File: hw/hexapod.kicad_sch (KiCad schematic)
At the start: 76 parts, among them J1 Supply Motor, J10 Conn_01x03_Pin, J11 Conn_01x03_Pin, J12 Conn_01x03_Pin, J13 Conn_01x03_Pin, J14 Conn_01x03_Pin, J15 Conn_01x03_Pin, J16 Conn_01x03_Pin, J17 Conn_01x03_Pin, J18 Conn_01x03_Pin, J19 Conn_01x03_Pin, J20 Conn_01x03_Pin, J21 Conn_01x03_Pin, J22 Conn_01x03_Pin, J23 Conn_01x03_Pin, J24 Conn_01x03_Pin, J25 Conn_01x03_Pin, J26 Conn_01x03_Pin, J27 Conn_01x03_Pin, J28 Conn_01x03_Pin, J29 Conn_01x03_Pin, J3 Conn_01x03_Pin, J30 Conn_01x03_Pin, J31 Conn_01x03_Pin, J32 Conn_01x03_Pin, J33 Conn_01x03_Pin, J34 Conn_01x03_Pin, J35 Conn_01x06_Pin, J4 Conn_01x03_Pin, J5 Conn_01x03_Pin, J6 Conn_01x03_Pin, J7 Conn_01x03_Pin, J8 Conn_01x03_Pin, J9 Conn_01x03_Pin, Q2 AOD417, U2 PCA9685PW, U3 PCA9685PW

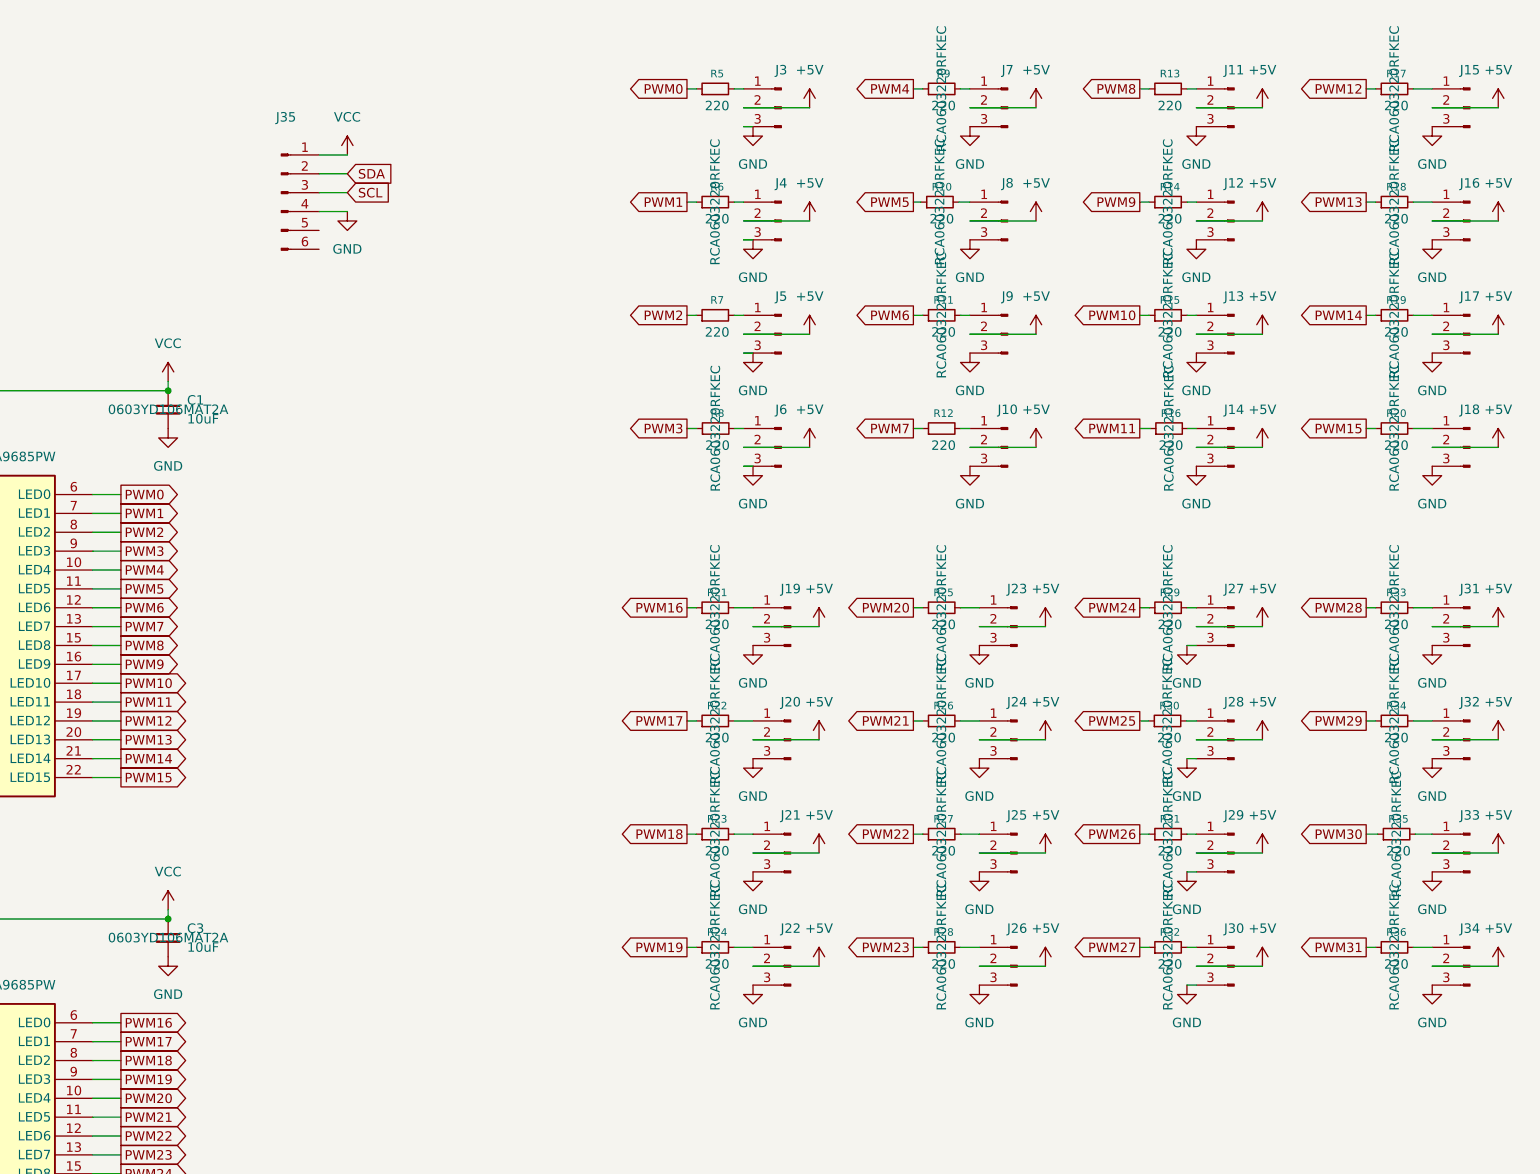
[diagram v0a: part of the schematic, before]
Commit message: hw: Keep only needed pwm
Signed-off-by: Florian Depraz <florian.depraz@outlook.com>
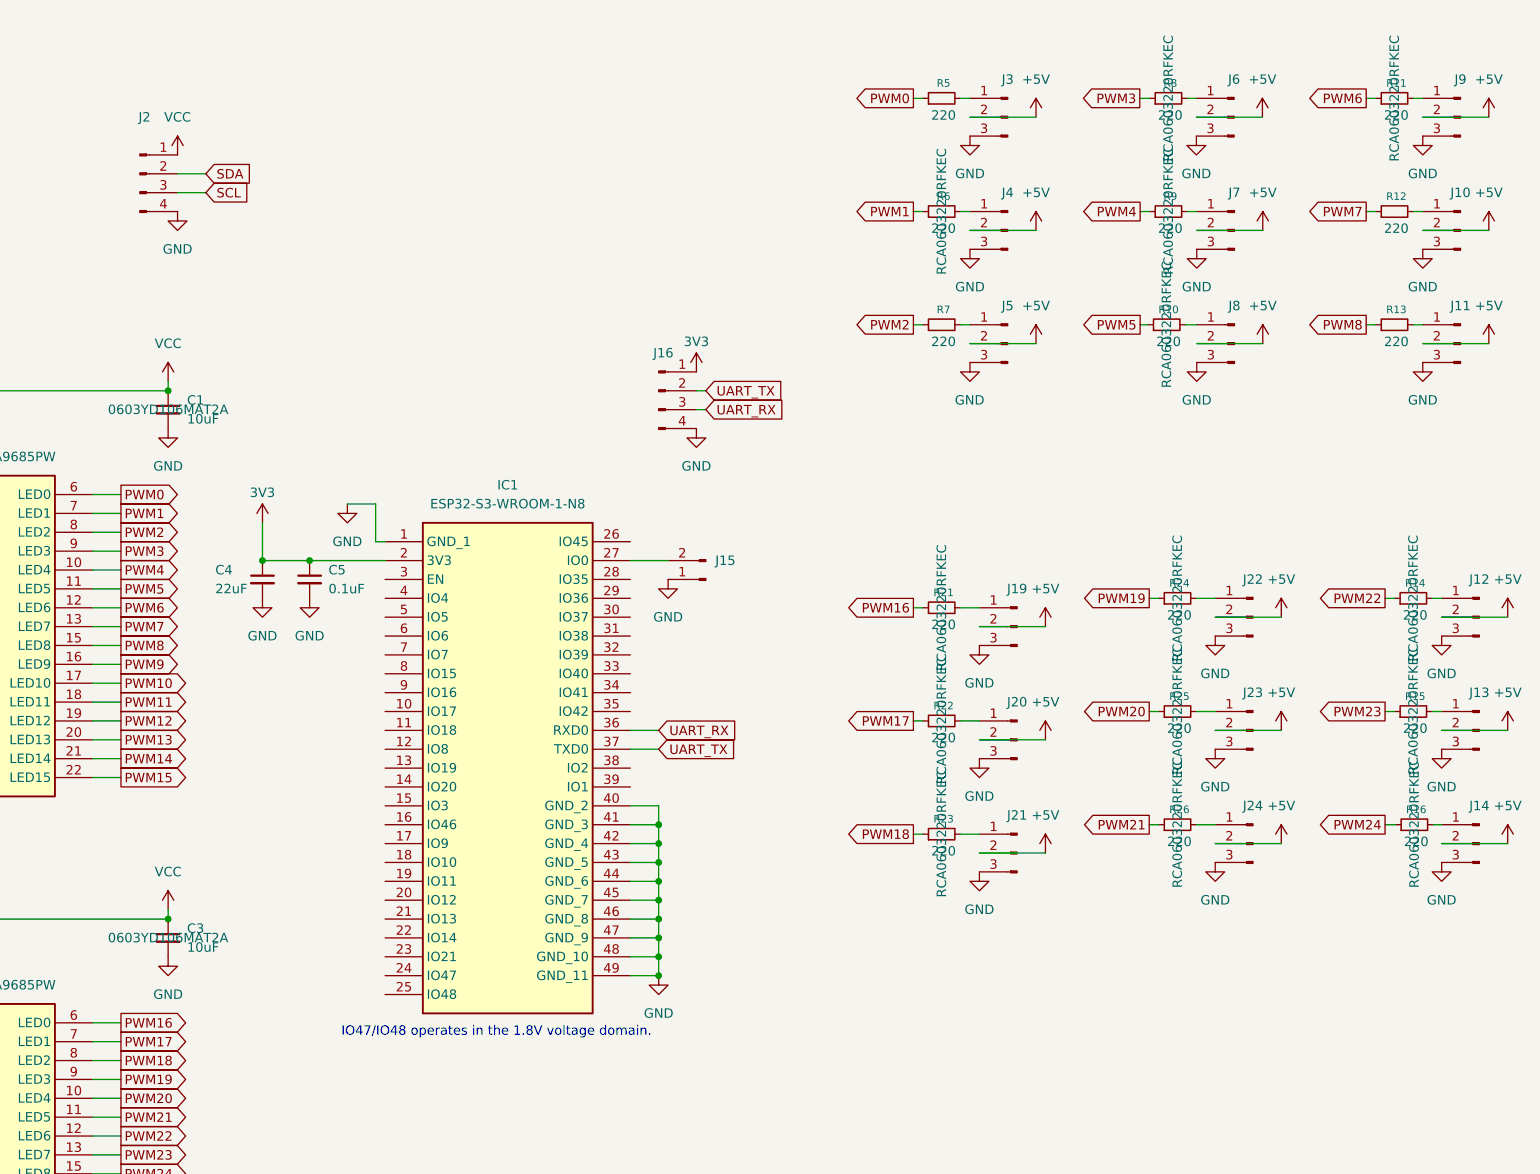
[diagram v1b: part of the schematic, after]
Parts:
- removed J15, J16, J17, J18, J25, J26, J27, J28, J29, J30, J31, J32, J33, J34: Conn_01x03_Pin, Connector_PinHeader_2.54mm:PinHeader_1x03_P2.54mm_Vertical, symbol Connector:Conn_01x03_Pin
- removed J35: Conn_01x06_Pin, Connector_PinHeader_2.54mm:PinHeader_1x06_P2.54mm_Vertical, symbol Connector:Conn_01x06_Pin
- removed R17, R18, R19, R20, R27, R28, R29, R30, R31, R32, R33, R34, R35, R36: 220, Resistor_SMD:R_0603_1608Metric_Pad0.98x0.95mm_HandSolder, symbol Device:R_Small
- added C4: 22uF, Capacitor_SMD:C_0603_1608Metric, symbol Device:C_Small
- added C5: 0.1uF, Capacitor_SMD:C_0603_1608Metric, symbol Device:C_Small
- added IC1: ESP32-S3-WROOM-1-N8, ESP32S3WROOM1N8R2, symbol ESP32-S3-WROOM-1-N8:ESP32-S3-WROOM-1-N8
- added J15: Conn_01x02_Pin, Connector_PinHeader_2.54mm:PinHeader_1x02_P2.54mm_Vertical, symbol Connector:Conn_01x02_Pin
- added J16, J2: Conn_01x04_Pin, Connector_PinHeader_2.54mm:PinHeader_1x04_P2.54mm_Vertical, symbol Connector:Conn_01x04_Pin
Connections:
- net GND: now also C4.2, C5.2, IC1.1 (GND_1), IC1.40 (GND_2), IC1.41 (GND_3), IC1.42 (GND_4), IC1.43 (GND_5), IC1.44 (GND_6), IC1.45 (GND_7), IC1.46 (GND_8), IC1.47 (GND_9), IC1.48 (GND_10), IC1.49 (GND_11), J15.1 (Pin_1), J16.4 (Pin_4), J2.4 (Pin_4)
- net PWM10: no longer R15.1
- net PWM11: no longer R16.1
- net PWM22: now also R14.1
- net PWM23: now also R15.1
- net PWM24: now also R16.1
- net PWM9: no longer R14.1
- net SCL: now also J2.3 (Pin_3)
- net SDA: now also J2.2 (Pin_2)
- net VCC: now also J2.1 (Pin_1)
- new net: IC1.27 (IO0), J15.2 (Pin_2)
- new net 3V3: C4.1, C5.1, IC1.2 (3V3), J16.1 (Pin_1)
- new net UART_RX: IC1.36 (RXD0), J16.3 (Pin_3)
- new net UART_TX: IC1.37 (TXD0), J16.2 (Pin_2)
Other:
- note added: "IO47/IO48 operates in the 1.8V voltage domain."
- moved on the sheet: J10, J11, J12, J13, J14, J19, J20, J21, J22, J23, J24, J3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

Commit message: hw: Add ESP32
Signed-off-by: Florian Depraz <florian.depraz@outlook.com>
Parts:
- removed C4: 22uF, Capacitor_SMD:C_0603_1608Metric, symbol Device:C_Small
- removed C5: 0.1uF, Capacitor_SMD:C_0603_1608Metric, symbol Device:C_Small
- removed IC1: ESP32-S3-WROOM-1-N8, ESP32S3WROOM1N8R2, symbol ESP32-S3-WROOM-1-N8:ESP32-S3-WROOM-1-N8
- removed J15: Conn_01x02_Pin, Connector_PinHeader_2.54mm:PinHeader_1x02_P2.54mm_Vertical, symbol Connector:Conn_01x02_Pin
- removed J16, J2: Conn_01x04_Pin, Connector_PinHeader_2.54mm:PinHeader_1x04_P2.54mm_Vertical, symbol Connector:Conn_01x04_Pin
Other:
- added sheet ESP32 (power.kicad_sch)
- note removed: "IO47/IO48 operates in the 1.8V voltage domain."
